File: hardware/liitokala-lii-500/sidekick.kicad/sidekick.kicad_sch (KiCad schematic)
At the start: 26 parts, among them J1 MCU, J2 USB, J3 LCD, J4 ST-Link V2, J5 EXPANSION, U1 STM32F103C8Tx, U2 XC6206PxxxMR, Y1 8 MHz

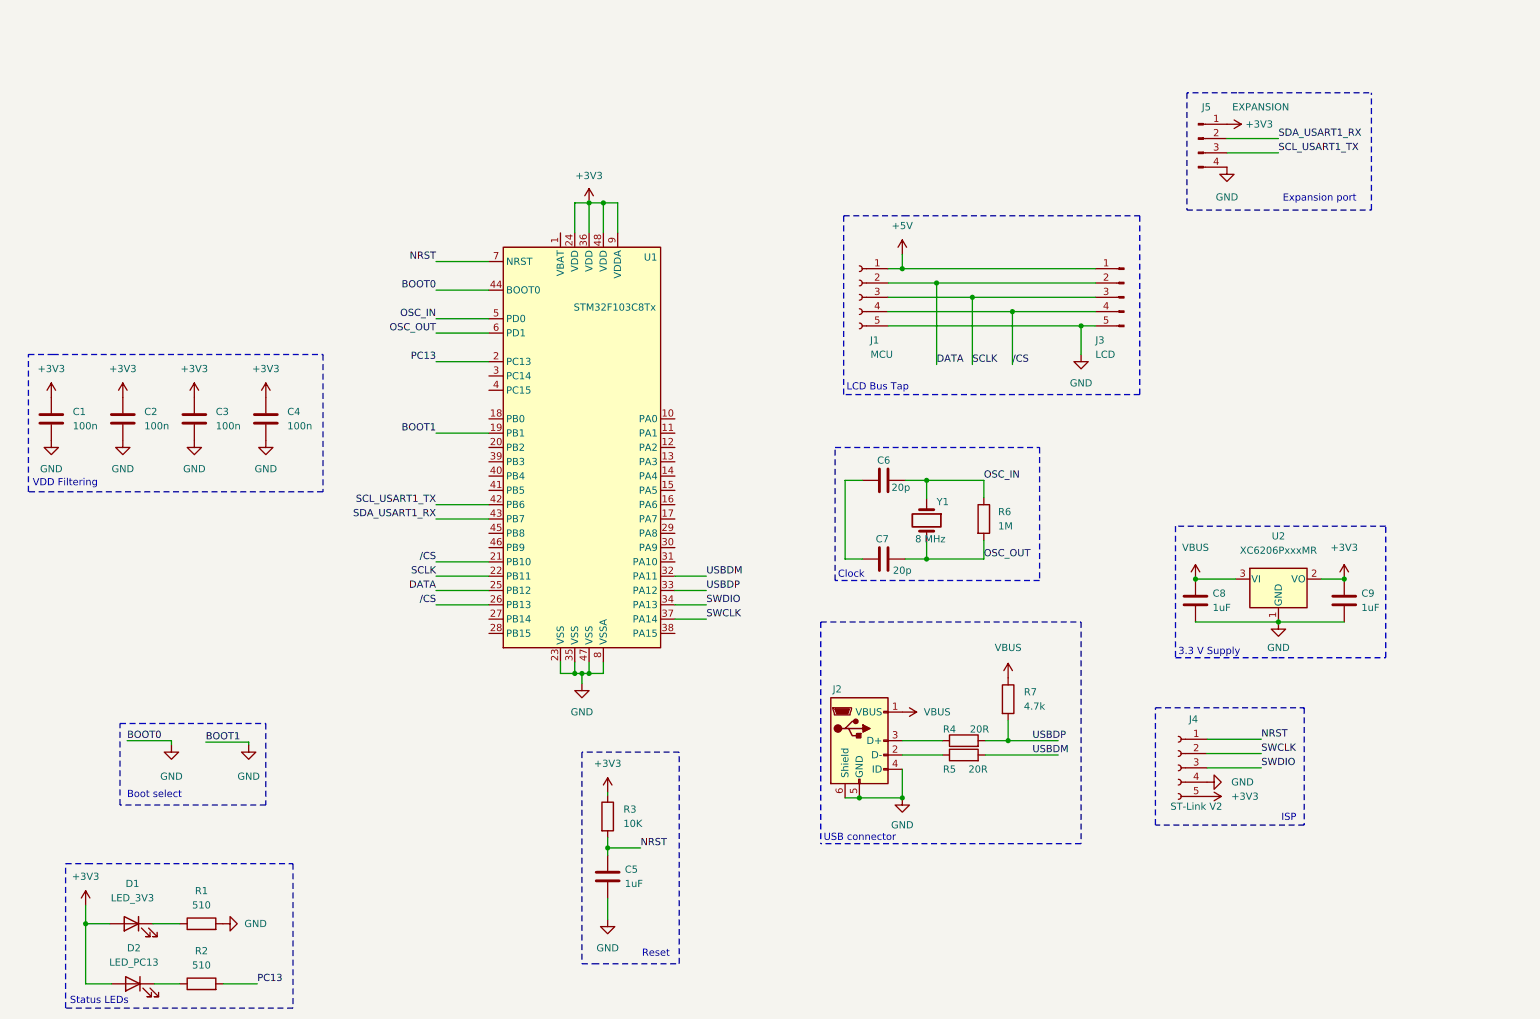
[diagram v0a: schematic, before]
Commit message: liitokala-lii500: Update current project files to rev 2
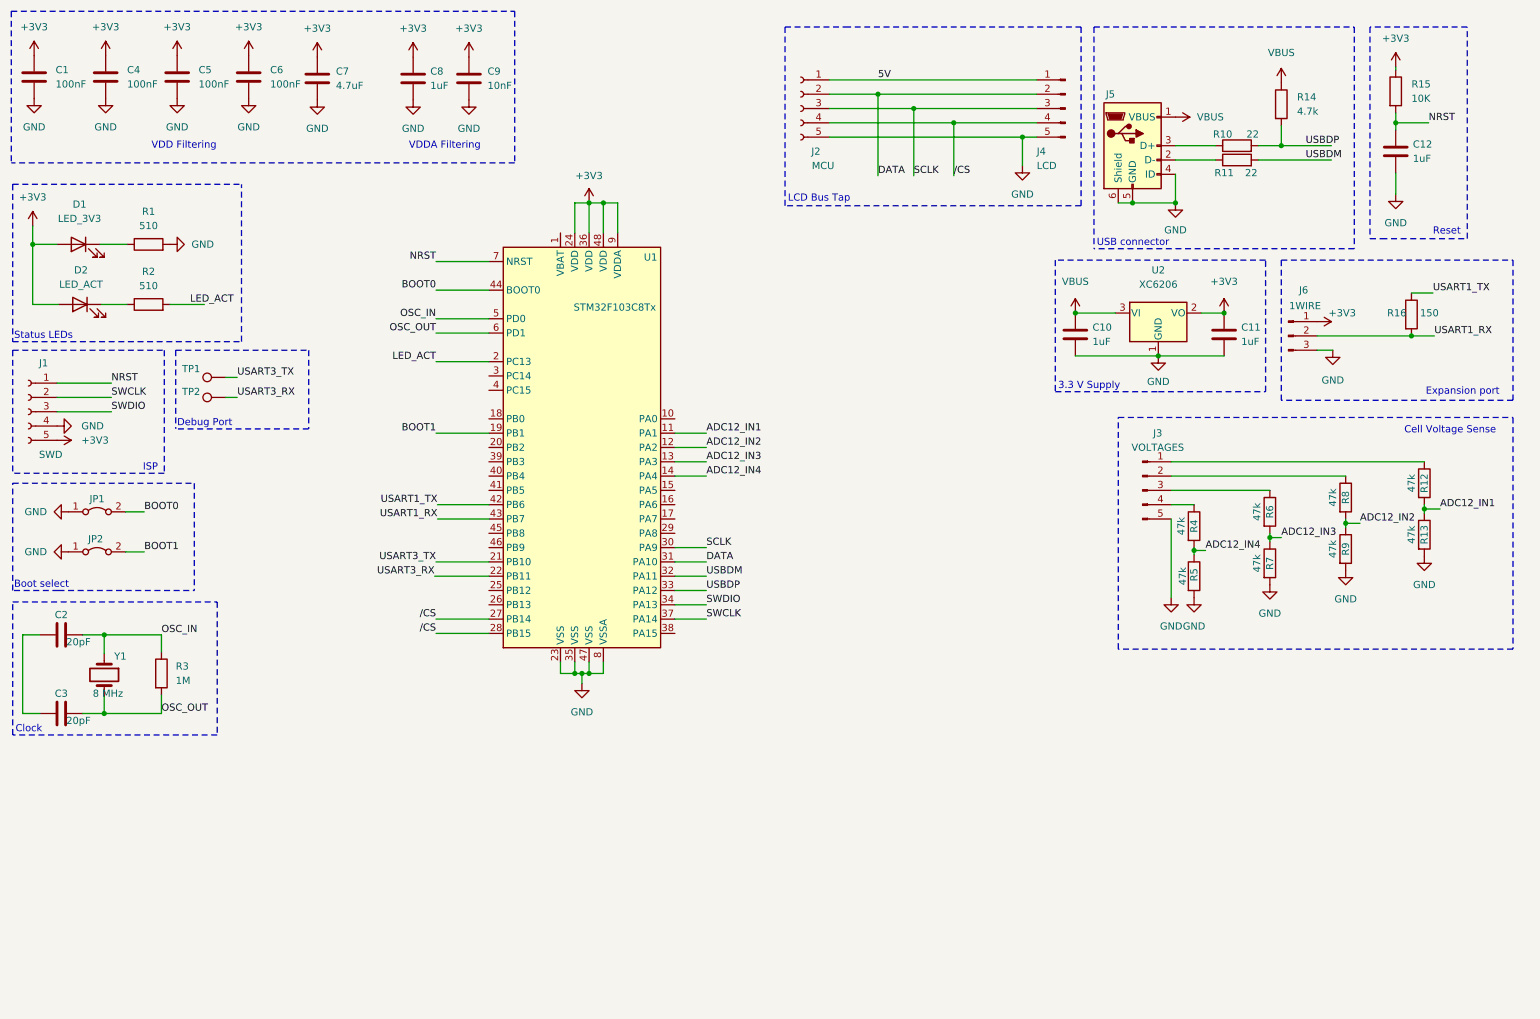
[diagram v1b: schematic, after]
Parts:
- removed C5: 1uF, Resistor_SMD:R_0603_1608Metric, symbol Device:C
- removed J5: EXPANSION, Connector_PinHeader_2.54mm:PinHeader_1x04_P2.54mm_Horizontal, symbol Connector:Conn_01x04_Male
- added C11, C12, C8: 1uF, Capacitor_SMD:C_0402_1005Metric, symbol Device:C
- added C3: 20pF, Capacitor_SMD:C_0402_1005Metric, symbol Device:C
- added J3: VOLTAGES, Connector_PinHeader_2.54mm:PinHeader_1x05_P2.54mm_Horizontal, symbol Connector:Conn_01x05_Male
- added J6: 1WIRE, Connector_PinHeader_2.54mm:PinHeader_1x03_P2.54mm_Horizontal, symbol Connector:Conn_01x03_Male
- added JP1, JP2: Jumper_2_Bridged, Jumper:SolderJumper-2_P1.3mm_Bridged_Pad1.0x1.5mm, symbol Jumper:Jumper_2_Bridged
- added R11: 22, Resistor_SMD:R_0402_1005Metric, symbol Device:R
- added R12, R13, R4, R6, R7, R8, R9: 47k, Resistor_SMD:R_0402_1005Metric, symbol Device:R
- added R16: 150, Resistor_SMD:R_0402_1005Metric, symbol Device:R
- added TP1, TP2: TestPoint, TestPoint:TestPoint_THTPad_D1.5mm_Drill0.7mm, symbol Connector:TestPoint
- C1: value 100n -> 100nF; footprint Capacitor_SMD:C_0603_1608Metric -> Capacitor_SMD:C_0402_1005Metric; JLCPCB Part # (none) -> C1525; MFR.Part # (none) -> CL05B104KO5NNNC; Manufacturer (none) -> Samsung Electro-Mechanics
- C10: renamed from C8; footprint Resistor_SMD:R_0603_1608Metric -> Capacitor_SMD:C_0402_1005Metric; JLCPCB Part # C15849 -> C52923; MFR.Part # CL10A105KB8NNNC -> CL05A105KA5NQNC
- C2: renamed from C6; value 20p -> 20pF; footprint Capacitor_SMD:C_0603_1608Metric -> Capacitor_SMD:C_0402_1005Metric; JLCPCB Part # C1648 -> C1554; MFR.Part # CL10C200JB8NNNC -> 0402CG200J500NT; Manufacturer (none) -> FH(Guangdong Fenghua Advanced Tech)
- C4: renamed from C2; value 100n -> 100nF; footprint Capacitor_SMD:C_0603_1608Metric -> Capacitor_SMD:C_0402_1005Metric; JLCPCB Part # (none) -> C1525; MFR.Part # (none) -> CL05B104KO5NNNC; Manufacturer (none) -> Samsung Electro-Mechanics
- C5: renamed from C3; value 100n -> 100nF; footprint Capacitor_SMD:C_0603_1608Metric -> Capacitor_SMD:C_0402_1005Metric; JLCPCB Part # (none) -> C1525; MFR.Part # (none) -> CL05B104KO5NNNC; Manufacturer (none) -> Samsung Electro-Mechanics
- C6: renamed from C4; value 100n -> 100nF; footprint Capacitor_SMD:C_0603_1608Metric -> Capacitor_SMD:C_0402_1005Metric; JLCPCB Part # (none) -> C1525; MFR.Part # (none) -> CL05B104KO5NNNC; Manufacturer (none) -> Samsung Electro-Mechanics
- C7: value 20p -> 4.7uF; footprint Capacitor_SMD:C_0603_1608Metric -> Capacitor_SMD:C_0805_2012Metric; JLCPCB Part # C1648 -> C1779; MFR.Part # CL10C200JB8NNNC -> CL21A475KAQNNNE; Manufacturer (none) -> Samsung Electro-Mechanics
- C9: value 1uF -> 10nF; footprint Resistor_SMD:R_0603_1608Metric -> Capacitor_SMD:C_0402_1005Metric; JLCPCB Part # C15849 -> C15195; MFR.Part # CL10A105KB8NNNC -> CL05B103KB5NNNC
- D2: value LED_PC13 -> LED_ACT
- J1: renamed from J4; value ST-Link V2 -> SWD
- R1, R2: footprint Resistor_SMD:R_0603_1608Metric -> Resistor_SMD:R_0402_1005Metric; JLCPCB Part # C23193 -> C25123; MFR.Part # 0603WAF5100T5E -> 0402WGF5100TCE
- R10: renamed from R4; value 20R -> 22; footprint Resistor_SMD:R_0603_1608Metric -> Resistor_SMD:R_0402_1005Metric; JLCPCB Part # C22950 -> C25092; MFR.Part # 0603WAF200JT5E -> 0402WGF220JTCE; Manufacturer Uniroyal Elec -> UNI-ROYAL(Uniroyal Elec)
- R14: renamed from R7; footprint Resistor_SMD:R_0603_1608Metric -> Resistor_SMD:R_0402_1005Metric; JLCPCB Part # C23162 -> C25900; MFR.Part # 0603WAF4701T5E -> 0402WGF4701TCE
- R15: renamed from R3; footprint Resistor_SMD:R_0603_1608Metric -> Resistor_SMD:R_0402_1005Metric; JLCPCB Part # C22797 -> C25744; MFR.Part # 0603WAF1302T5E -> 0402WGF1002TCE
- R3: renamed from R6; footprint Resistor_SMD:R_0603_1608Metric -> Resistor_SMD:R_0402_1005Metric; JLCPCB Part # C22935 -> C26083; MFR.Part # 0603WAF1004T5E -> 0402WGF1004TCE; Manufacturer (none) -> UNI-ROYAL(Uniroyal Elec)
- R5: value 20R -> 47k; footprint Resistor_SMD:R_0603_1608Metric -> Resistor_SMD:R_0402_1005Metric; JLCPCB Part # C22950 -> C25792; MFR.Part # 0603WAF200JT5E -> 0402WGF4702TCE; Manufacturer Uniroyal Elec -> UNI-ROYAL(Uniroyal Elec)
- U1: JLCPCB Part # (none) -> C8734; MFR.Part # (none) -> STM32F103C8T6; Manufacturer (none) -> STMicroelectronics
- U2: value XC6206PxxxMR -> XC6206; JLCPCB Part # (none) -> C5446; MFR.Part # (none) -> XC6206P332MR; Manufacturer (none) -> Torex Semicon
- Y1: MFR.Part # (none) -> X49SM8MSB2SC; Manufacturer (none) -> Yangxing Tech
- renumbered J1 to J2, J3 to J4, J2 to J5
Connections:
- net +3V3: now also C7.1, C11.1, C8.1, J6.1 (Pin_1)
- net DATA: now also U1.31 (PA10); no longer U1.25 (PB12)
- net GND: now also C7.2, R5.2, C11.2, C12.2, C8.2, J3.5 (Pin_5), J6.3 (Pin_3), JP1.1 (A), JP2.1 (A), R13.2, R7.2, R9.2; no longer U1.19 (PB1), U1.44 (BOOT0)
- net NRST: now also C12.1
- net OSC_OUT: now also C3.2; no longer C7.2
- net SCLK: now also U1.30 (PA9); no longer U1.22 (PB11)
- net USBDM: now also R11.2; no longer R5.2
- net /CS: now also U1.27 (PB14), U1.28 (PB15); no longer U1.21 (PB10), U1.26 (PB13)
- net ADC12_IN1: now reaches U1.11 (PA1)
- net ADC12_IN1: now also R12.2, R13.1
- net ADC12_IN2: now reaches U1.12 (PA2)
- net ADC12_IN2: now also R8.2, R9.1
- net ADC12_IN3: now reaches U1.13 (PA3)
- net ADC12_IN3: now also R6.2, R7.1
- net ADC12_IN4: now reaches U1.14 (PA4)
- net ADC12_IN4: now also R5.1, R4.2
- net at J5.2 (D-): now also R11.1; no longer R5.1
- net at C2.1: now also C3.1; no longer C7.1
- net +5V renamed 5V
- net PC13 renamed LED_ACT
- net SCL_USART1_TX renamed USART1_TX
- net USART1_TX: now also R16.1
- net SDA_USART1_RX renamed USART1_RX
- net USART1_RX: now also J6.2 (Pin_2), R16.2
- new net: J3.4 (Pin_4), R4.1
- new net: J3.2 (Pin_2), R8.1
- new net: J3.3 (Pin_3), R6.1
- new net: J3.1 (Pin_1), R12.1
- new net BOOT0: JP1.2 (B), U1.44 (BOOT0)
- new net BOOT1: JP2.2 (B), U1.19 (PB1)
- new net USART3_RX: TP2.1, U1.22 (PB11)
- new net USART3_TX: TP1.1, U1.21 (PB10)
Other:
- note added: "Cell Voltage Sense"
- note added: "Debug Port"
- note added: "VDDA Filtering"
- company: SHILL.GQ -> FSCK.PL
- title: Charger Sidekick -> LII-500 Charger Sidekick 
- moved on the sheet: C1, C10, C2, C4, C5, C6, D1, D2, J1, J2, J4, J5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

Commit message: liitokala-lii500: Updated kicad files to rev 3
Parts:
- removed J6: 1WIRE, Connector_PinHeader_2.54mm:PinHeader_1x03_P2.54mm_Horizontal, symbol Connector:Conn_01x03_Male
- added D3, D4: SM4007PL, Diode_SMD:D_SOD-123, symbol Device:D
- added J6: EXPAND, Connector_PinHeader_2.54mm:PinHeader_1x04_P2.54mm_Horizontal, symbol Connector:Conn_01x04_Male
- added R17, R18: 10K, Resistor_SMD:R_0402_1005Metric, symbol Device:R
- J5: footprint Local:JUSHUO_AFC07-S05ECC-00_1x05_1MP_P0.5mm_Horizontal -> Local:JUSHUO_ AFA07-S05FCC-00_1x05_1MP_P1mm_Horizontal; JLCPCB Part # C262230 -> C262339; MFR.Part # AFC07-S05ECC-00 -> AFA07-S05FCC-00
- Y1: footprint Crystal:Crystal_SMD_HC49-SD -> Crystal:Crystal_SMD_5032-2Pin_5.0x3.2mm; JLCPCB Part # C108703 -> C115962; MFR.Part # X49SM8MSB2SC -> X50328MSB2GI
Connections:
- net +3V3: now also J6.1 (Pin_1), R17.1, R18.1
- net 5V: now also D3.2 (A)
- net DATA: now also U1.28 (PB15); no longer U1.31 (PA10)
- net GND: now also J6.4 (Pin_4); no longer J5.4 (ID)
- net SCLK: now also U1.29 (PA8); no longer U1.30 (PA9)
- net USART1_RX: now also J6.3 (Pin_3), R18.2
- net USART1_TX: now also J6.2 (Pin_2), R17.2
- net VBUS: now also D4.2 (A); no longer C10.1, U2.3 (VI)
- net /CS: now also U1.30 (PA9), U1.31 (PA10); no longer U1.27 (PB14), U1.28 (PB15)
- new net +5V: C10.1, D3.1 (K), D4.1 (K), U2.3 (VI)
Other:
- moved on the sheet: C10, C11, C2, C3, D1, D2, J1, J3, JP1, JP2, R1, R12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

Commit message: liitokala-lii500: Add rev3 board files
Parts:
- added R19, R20, R21, R22, R23: 470R, Resistor_SMD:R_0402_1005Metric, symbol Device:R
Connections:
- net DATA: now also R21.2; no longer J2.2 (Pin_2), J4.2 (Pin_2)
- net SCLK: now also R22.2; no longer J2.3 (Pin_3), J4.3 (Pin_3)
- net USART3_RX: now also R20.2; no longer TP2.1
- net USART3_TX: now also R19.2; no longer TP1.1
- net /CS: now also R23.2; no longer J2.4 (Pin_4), J4.4 (Pin_4)
- new net: J2.2 (Pin_2), J4.2 (Pin_2), R21.1
- new net: J2.3 (Pin_3), J4.3 (Pin_3), R22.1
- new net: J2.4 (Pin_4), J4.4 (Pin_4), R23.1
- new net: R20.1, TP2.1
- new net: R19.1, TP1.1

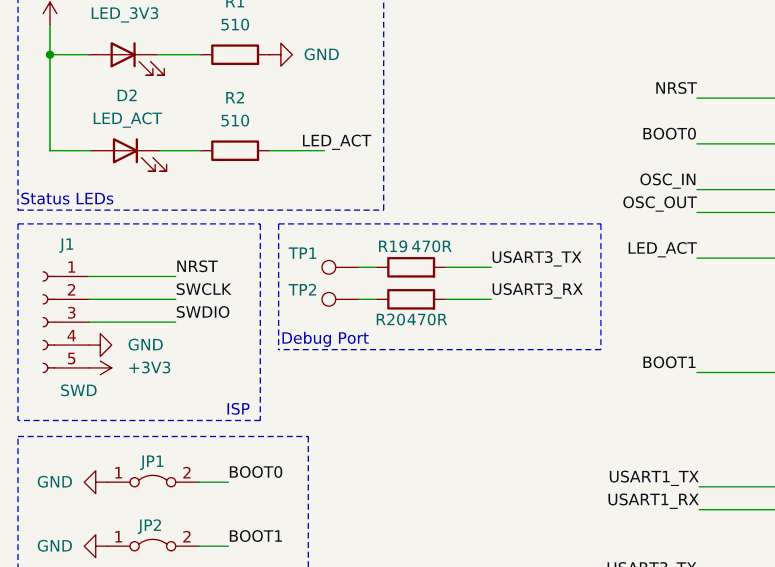
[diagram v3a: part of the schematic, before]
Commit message: liitokala-lii500: Make debug UART pad labels more distinctive
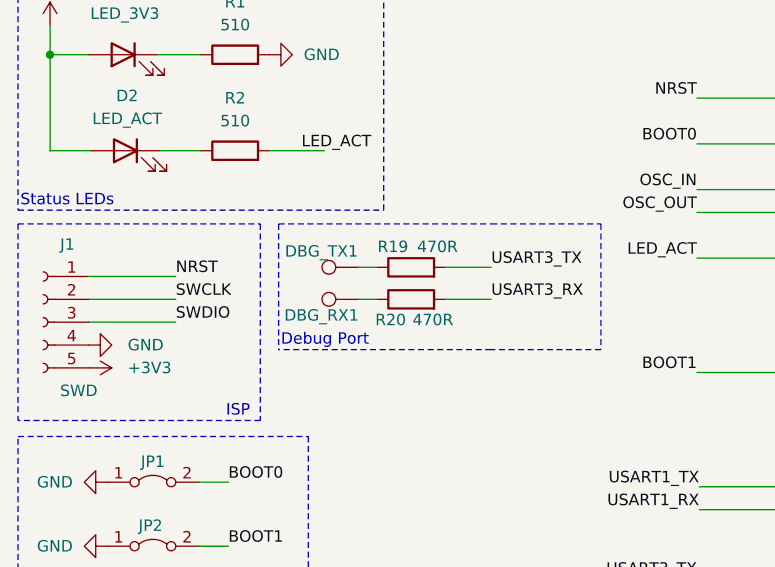
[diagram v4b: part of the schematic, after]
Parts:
- renumbered TP2 to DBG_RX1, TP1 to DBG_TX1
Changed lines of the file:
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@@
   (symbol (lib_id "Connector:TestPoint") (at 52.324 77.216 90) (unit 1)
     (in_bom yes) (on_board yes)
-    (property "Reference" "TP1" (id 0) (at 46.1645 75.692 90))
+    (property "Reference" "DBG_TX1" (id 0) (at 48.1965 75.438 90))
     (property "Value" "TestPoint" (id 1) (at 51.7524 75.438 0)
       (effects (font (size 1.27 1.27)) (justify left) hide)
@@
   (symbol (lib_id "Connector:TestPoint") (at 52.324 80.772 90) (unit 1)
     (in_bom yes) (on_board yes)
-    (property "Reference" "TP2" (id 0) (at 46.1645 79.756 90))
+    (property "Reference" "DBG_RX1" (id 0) (at 48.1965 82.55 90))
     (property "Value" "TestPoint" (id 1) (at 51.7524 78.994 0)
       (effects (font (size 1.27 1.27)) (justify left) hide)
@@
     (in_bom yes) (on_board yes)
     (property "Reference" "R19" (id 0) (at 56.134 74.93 90))
-    (property "Value" "470R" (id 1) (at 60.452 74.93 90))
+    (property "Value" "470R" (id 1) (at 61.087 74.93 90))
     (property "Footprint" "Resistor_SMD:R_0402_1005Metric" (id 2) (at 58.166 78.994 90)
       (effects (font (size 1.27 1.27)) hide)
@@
     (in_bom yes) (on_board yes)
     (property "Reference" "R20" (id 0) (at 55.88 83.058 90))
-    (property "Value" "470R" (id 1) (at 59.944 83.058 90))
+    (property "Value" "470R" (id 1) (at 60.579 83.058 90))
     (property "Footprint" "Resistor_SMD:R_0402_1005Metric" (id 2) (at 58.166 82.55 90)
       (effects (font (size 1.27 1.27)) hide)
@@
       (reference "D4") (unit 1) (value "SM4007PL") (footprint "Diode_SMD:D_SOD-123")
     )
+    (path "/890eab3a-781c-43e1-b7ce-2de856324386"
+      (reference "DBG_RX1") (unit 1) (value "TestPoint") (footprint "TestPoint:TestPoint_THTPad_D1.5mm_Drill0.7mm")
+    )
+    (path "/ac472d7f-9a68-4982-8a16-9de6850df04b"
+      (reference "DBG_TX1") (unit 1) (value "TestPoint") (footprint "TestPoint:TestPoint_THTPad_D1.5mm_Drill0.7mm")
+    )
     (path "/2c629b67-2e41-4a7c-80df-ad705a3ed155"
       (reference "J1") (unit 1) (value "SWD") (footprint "Connector_PinHeader_2.54mm:PinHeader_1x05_P2.54mm_Vertical")
@@
       (reference "R23") (unit 1) (value "470R") (footprint "Resistor_SMD:R_0402_1005Metric")
     )
-    (path "/ac472d7f-9a68-4982-8a16-9de6850df04b"
-      (reference "TP1") (unit 1) (value "TestPoint") (footprint "TestPoint:TestPoint_THTPad_D1.5mm_Drill0.7mm")
-    )
-    (path "/890eab3a-781c-43e1-b7ce-2de856324386"
-      (reference "TP2") (unit 1) (value "TestPoint") (footprint "TestPoint:TestPoint_THTPad_D1.5mm_Drill0.7mm")
-    )
     (path "/43a76c0f-f98c-49b4-bb45-972169417cdc"
